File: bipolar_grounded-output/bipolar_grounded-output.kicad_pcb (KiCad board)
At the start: 4 copper layers, 100 x 100 mm, 18 parts, among them J1 Conn_01x10_Pin, J10 Conn_Coaxial, J11 Conn_Coaxial, J12 Conn_01x04_Pin, J2 Conn_01x10_Pin, J3 Conn_01x04_Pin, J4 Conn_01x05, J5 Conn_01x03, J6 Conn_Coaxial, J7 Conn_Coaxial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

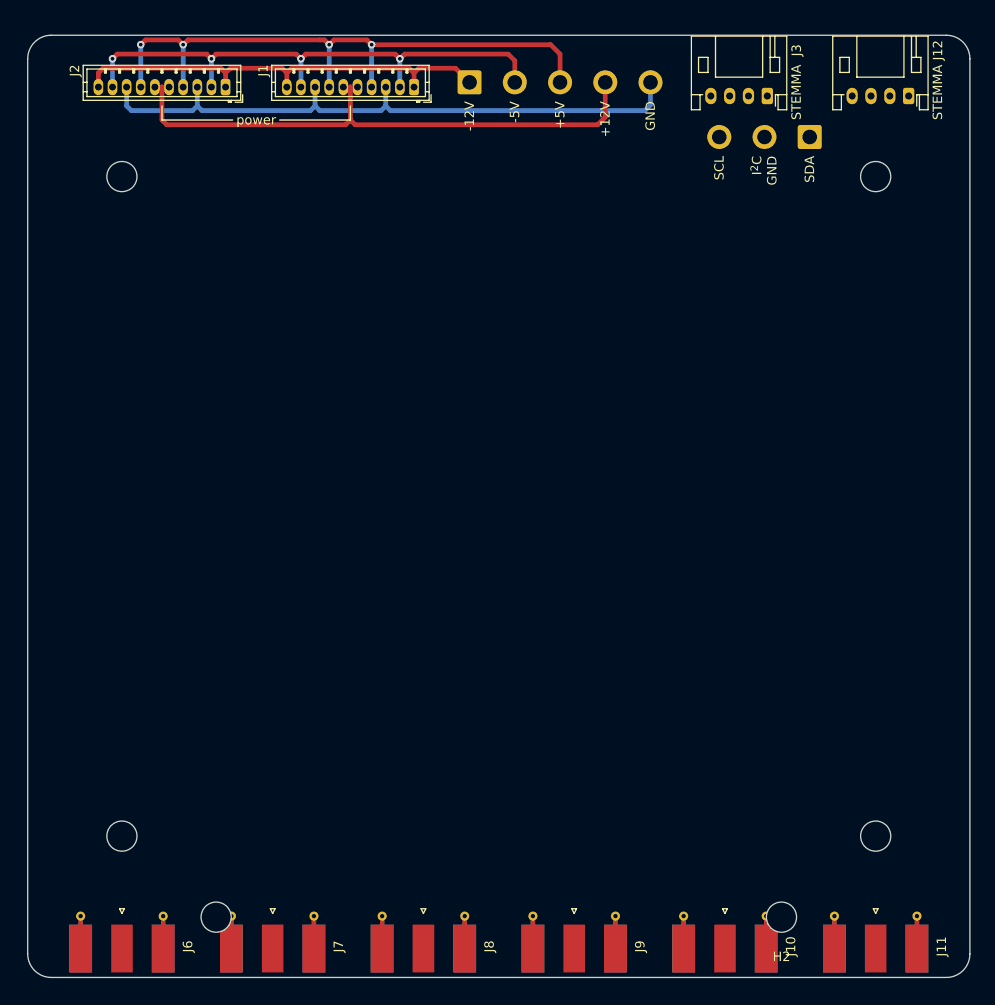
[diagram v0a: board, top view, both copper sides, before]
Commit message: layout PCB for grounded bipolar
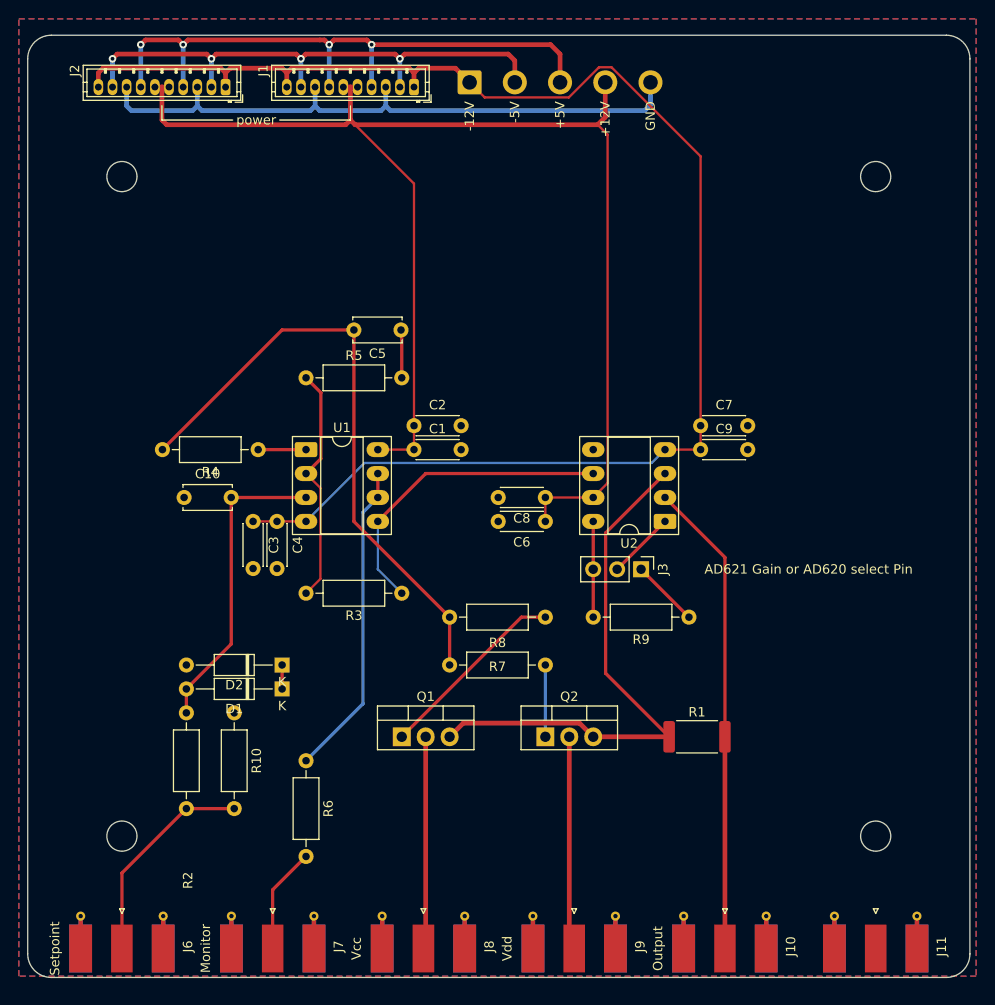
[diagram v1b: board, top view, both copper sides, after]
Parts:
- removed H1, H2: Keystone Electronics 621, matterwaves:Keystone 621
- removed J12: Conn_01x04_Pin, Connector_JST:JST_PH_S4B-PH-K_1x04_P2.00mm_Horizontal
- removed J5: Conn_01x03, Connector_Wire:SolderWire-0.75sqmm_1x03_P4.8mm_D1.25mm_OD2.3mm
- added C1: 100n, Capacitor_THT:C_Disc_D4.3mm_W1.9mm_P5.00mm, F.Cu at (141.0, 94.0)
- added C10: 1n, Capacitor_THT:C_Disc_D5.0mm_W2.5mm_P5.00mm, F.Cu at (116.6, 99.1)
- added C2: 10u, Capacitor_THT:C_Disc_D4.3mm_W1.9mm_P5.00mm, F.Cu at (141.0, 91.4)
- added C3: 10u, Capacitor_THT:C_Disc_D4.3mm_W1.9mm_P5.00mm, F.Cu at (123.9, 101.6)
- added C4: 100n, Capacitor_THT:C_Disc_D4.3mm_W1.9mm_P5.00mm, F.Cu at (126.5, 101.6)
- added C5: 10p, Capacitor_THT:C_Disc_D5.0mm_W2.5mm_P5.00mm, F.Cu at (139.6, 81.3)
- added C6: 10u, Capacitor_THT:C_Disc_D4.3mm_W1.9mm_P5.00mm, F.Cu at (154.9, 101.6)
- added C7: 10u, Capacitor_THT:C_Disc_D4.3mm_W1.9mm_P5.00mm, F.Cu at (171.4, 91.4)
- added C8: 100n, Capacitor_THT:C_Disc_D4.3mm_W1.9mm_P5.00mm, F.Cu at (154.9, 99.1)
- added C9: 100n, Capacitor_THT:C_Disc_D4.3mm_W1.9mm_P5.00mm, F.Cu at (171.4, 94.0)
- added D1: 10V, Diode_THT:D_DO-35_SOD27_P10.16mm_Horizontal, F.Cu at (127.0, 119.4)
- added D2: 10V, Diode_THT:D_DO-35_SOD27_P10.16mm_Horizontal, F.Cu at (127.0, 116.8)
- added Q1: TIP41C, Package_TO_SOT_THT:TO-220-3_Vertical, F.Cu at (139.7, 124.5)
- added Q2: TIP42C, Package_TO_SOT_THT:TO-220-3_Vertical, F.Cu at (154.9, 124.5)
- added R1: 100mOhm, Resistor_SMD:R_2512_6332Metric, F.Cu at (171.0, 124.5)
- added R10: 1k, Resistor_THT:R_Axial_DIN0207_L6.3mm_D2.5mm_P10.16mm_Horizontal, F.Cu at (121.9, 121.9)
- added R2: 1k, Resistor_THT:R_Axial_DIN0207_L6.3mm_D2.5mm_P10.16mm_Horizontal, F.Cu at (116.8, 132.1)
- added R3: 10k, Resistor_THT:R_Axial_DIN0207_L6.3mm_D2.5mm_P10.16mm_Horizontal, F.Cu at (139.7, 109.2)
- added R4: 5.1R, Resistor_THT:R_Axial_DIN0207_L6.3mm_D2.5mm_P10.16mm_Horizontal, F.Cu at (124.5, 94.0)
- added R5: 1k, Resistor_THT:R_Axial_DIN0207_L6.3mm_D2.5mm_P10.16mm_Horizontal, F.Cu at (129.5, 86.4)
- added R6: 100R, Resistor_THT:R_Axial_DIN0207_L6.3mm_D2.5mm_P10.16mm_Horizontal, F.Cu at (129.5, 127.0)
- added R7: 100R, Resistor_THT:R_Axial_DIN0207_L6.3mm_D2.5mm_P10.16mm_Horizontal, F.Cu at (144.8, 111.8)
- added R8: 100R, Resistor_THT:R_Axial_DIN0207_L6.3mm_D2.5mm_P10.16mm_Horizontal, F.Cu at (144.8, 116.8)
- added R9: 510R, Resistor_THT:R_Axial_DIN0207_L6.3mm_D2.5mm_P10.16mm_Horizontal, F.Cu at (170.2, 111.8)
- added U1: AD823, Package_DIP:DIP-8_W7.62mm_Socket_LongPads, F.Cu at (129.5, 94.0)
- added U2: AD620, Package_DIP:DIP-8_W7.62mm_Socket_LongPads, F.Cu at (167.6, 101.6)
- J10: value Conn_Coaxial -> Output
- J3: value Conn_01x04_Pin -> AD621 Gain or AD620 select Pin; footprint Connector_JST:JST_PH_S4B-PH-K_1x04_P2.00mm_Horizontal -> Connector_PinHeader_2.54mm:PinHeader_1x03_P2.54mm_Vertical
- J6: value Conn_Coaxial -> Setpoint
- J7: value Conn_Coaxial -> Monitor
- J8: value Conn_Coaxial -> Vcc
- J9: value Conn_Coaxial -> Vdd
- moved J3 52.0 mm to (165.1, 106.7), turned to -90 degrees
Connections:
- J10 pad 1: unconnected-(J10-In-Pad1) -> /measure-
- J10 pad 2: unconnected-(J10-Ext-Pad2) -> GND
- J3 pad 1: /I2C_SCL -> Net-(J3-Pin_1)
- J3 pad 2: /I2C_SDA -> Net-(J3-Pin_2)
- J3 pad 3: VBUS -> Net-(J3-Pin_3)
- J6 pad 1: unconnected-(J6-In-Pad1) -> Net-(J6-In)
- J6 pad 2: unconnected-(J6-Ext-Pad2) -> GND
- J7 pad 1: unconnected-(J7-In-Pad1) -> Net-(J7-In)
- J7 pad 2: unconnected-(J7-Ext-Pad2) -> GND
- J8 pad 1: unconnected-(J8-In-Pad1) -> Net-(J8-In)
- J8 pad 2: unconnected-(J8-Ext-Pad2) -> GND
- J9 pad 1: unconnected-(J9-In-Pad1) -> Net-(J9-In)
- J9 pad 2: unconnected-(J9-Ext-Pad2) -> GND
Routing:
- net -12V: track 47.5 -> 159.7 mm
- net +12V: track 61.7 -> 150.9 mm
- net Net-(C5-Pad2): track 0.00 -> 65.3 mm
- net /measure+: track 0.00 -> 57.8 mm
- net /measure-: track 0.00 -> 50.5 mm
- net Net-(U1B--IN): track 0.00 -> 33.6 mm
- net /signal: track 0.00 -> 33.6 mm
- net Net-(D1-A): track 0.00 -> 32.8 mm
- net /I2C_SCL: track 28.5 -> 0.00 mm
- net Net-(U1A--IN): track 0.00 -> 25.4 mm
- net Net-(J6-In): track 0.00 -> 22.8 mm
- net Net-(J9-In): track 0.00 -> 22.7 mm
- net Net-(J8-In): track 0.00 -> 22.6 mm
- net Net-(Q1-B): track 0.00 -> 20.5 mm
- net /I2C_SDA: track 20.5 -> 0.00 mm
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- added copper zone on B.Cu, net GND
- added copper zone on F.Cu, net GND
- added copper zone on In1.Cu, net GND
- added copper zone on In2.Cu, net GND
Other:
- board text added: "Bipolar Current Control"
- board text added: "Cavity AI, Mueller Group, UC Berkeley"
- board text removed: "CIRCUIT NAME"
- board text removed: "I^{2}C GND"
- board text removed: "J Roth, Mueller Group, UC Berkeley"
- board text removed: "SCL"
- board text removed: "SDA"
- board text removed: "STEMMA"
